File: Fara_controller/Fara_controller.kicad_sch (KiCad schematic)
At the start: 25 parts, among them U1 XL1509-12, U2 LDD-700L, U3 LDD-700L, U4 LDD-700L, U5 LDD-700L, X1 Conn_01x02, X10 Conn_01x02, X11 Conn_01x02, X2 Conn_01x02, X3 Fan_3pin, X4 Fan_3pin, X5 Fan_3pin, X6 Fan_3pin, X7 Joystick, X8 Conn_01x02, X9 Conn_01x02

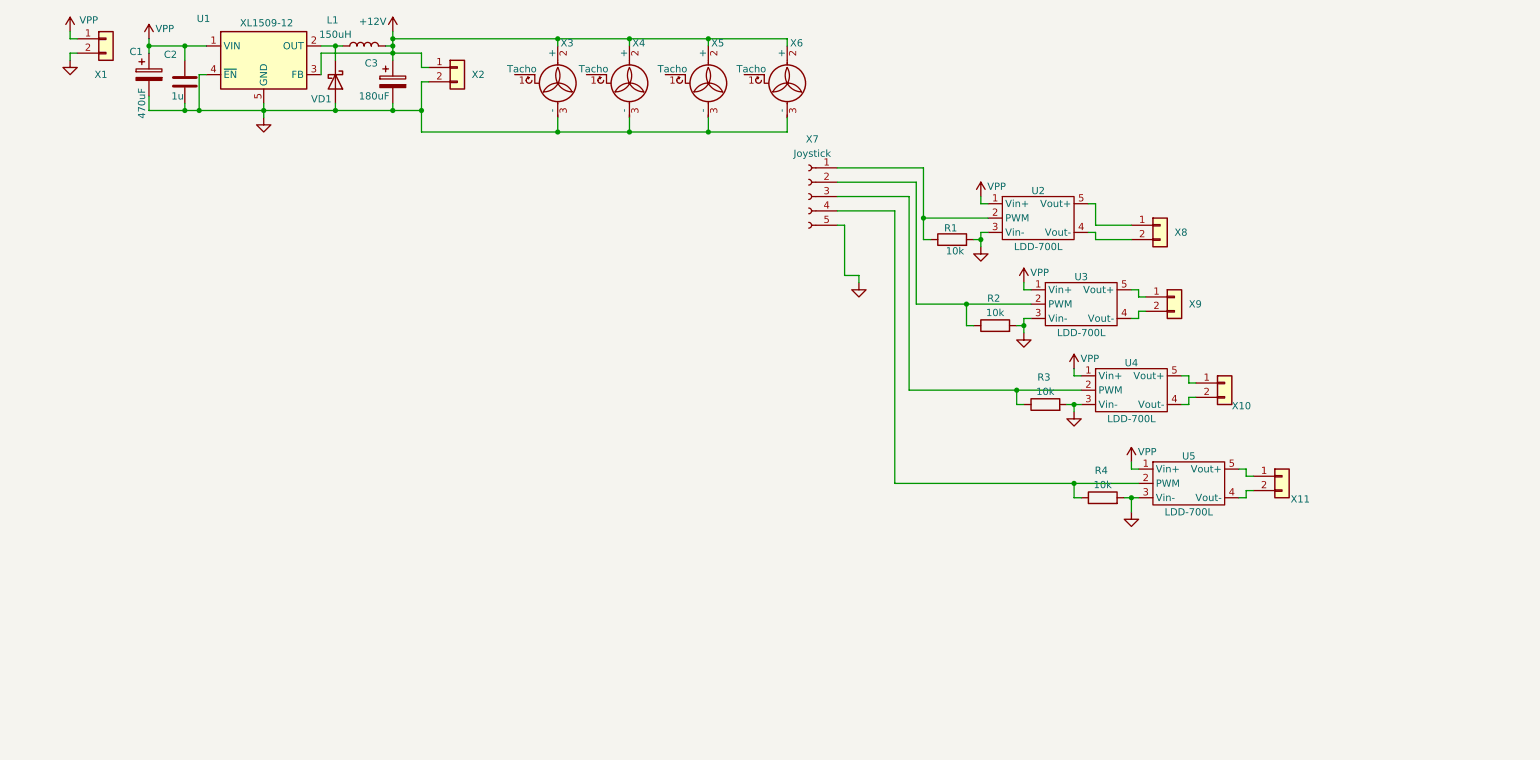
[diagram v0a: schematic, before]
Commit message: v0.2 draft routing of the 24V edition
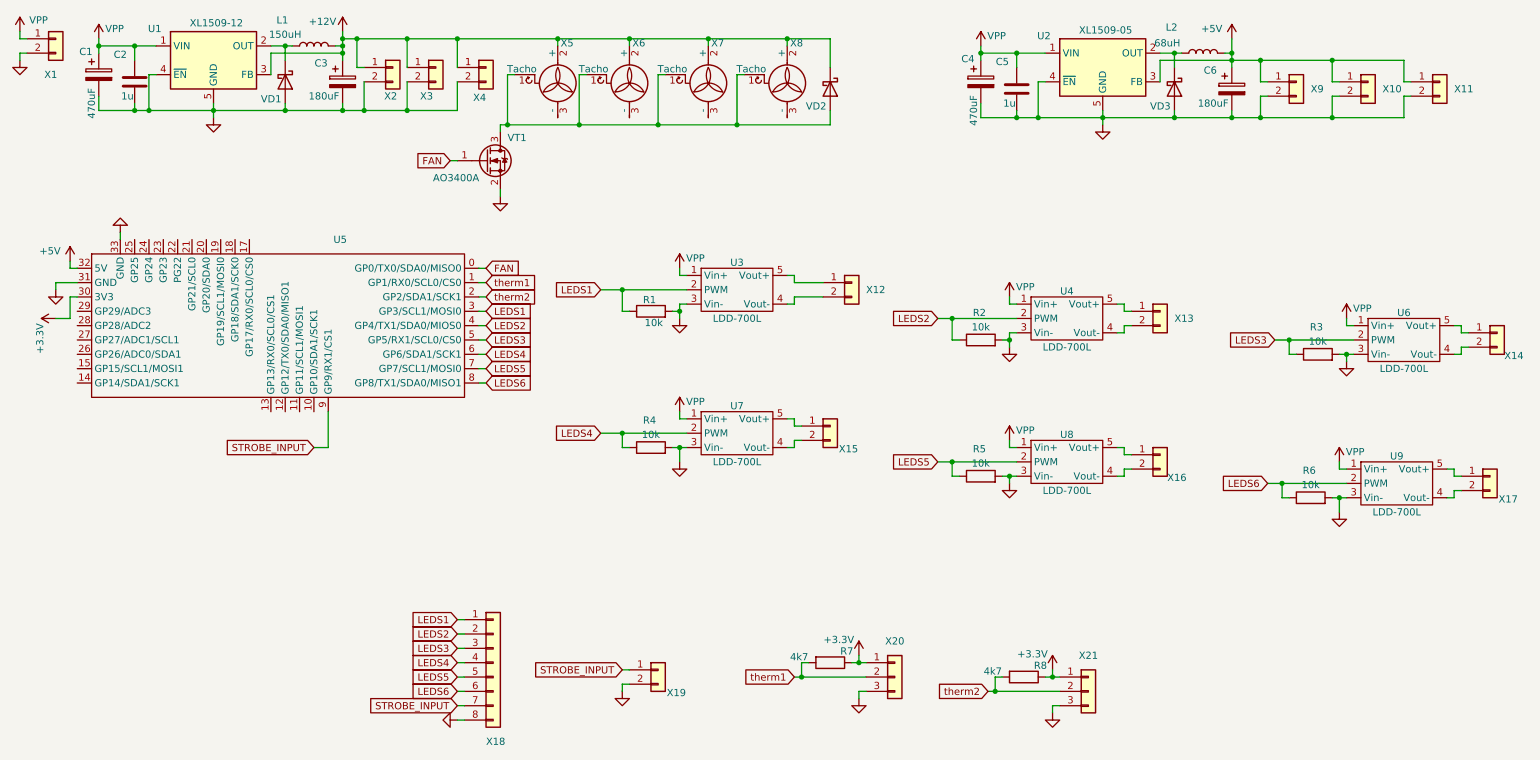
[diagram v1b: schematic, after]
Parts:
- removed X7: Joystick, Connector_JST:JST_XH_B5B-XH-A_1x05_P2.50mm_Vertical, symbol Connector:Conn_01x05_Female
- added C4: 470uF, Capacitor_THT:CP_Radial_D10.0mm_P5.00mm, symbol Device:C_Polarized
- added C5: 1u, Capacitor_SMD:C_0603_1608Metric_Pad1.08x0.95mm_HandSolder, symbol Device:C
- added C6: 180uF, Capacitor_SMD:CP_Elec_6.3x7.7, symbol Device:C_Polarized
- added L2: 68uH, Inductor_SMD:L_Bourns_SRP1050WA, symbol Device:L
- added R5, R6: 10k, Resistor_SMD:R_0603_1608Metric_Pad0.98x0.95mm_HandSolder, symbol Device:R
- added R7, R8: 4k7, Resistor_SMD:R_0603_1608Metric_Pad0.98x0.95mm_HandSolder, symbol Device:R
- added U2: XL1509-05, Package_SO:SOIC-8-1EP_3.9x4.9mm_P1.27mm_EP2.95x4.9mm_Mask2.71x3.4mm_ThermalVias, symbol My_8_lib_sym:XL1509-3.3
- added U5: ~, my8lib:RP2040Zero, symbol Vedro:RP2040-One
- added U8, U9: LDD-700L, my8lib:LDD-700L, symbol Shield_Emergent:LDD-700L
- added VD2, VD3: CDBA3100-HF, Diode_SMD:D_SMA, symbol Diode:CDBA3100-HF
- added VT1: AO3400A, Package_TO_SOT_SMD:SOT-23, symbol Transistor_FET:AO3400A
- added X10, X11, X16, X17, X19, X3, X4, X9: Conn_01x02, Connector_JST:JST_XH_B2B-XH-A_1x02_P2.50mm_Vertical, symbol Connector_Generic:Conn_01x02
- added X18: Objective, Connector_PinSocket_1.27mm:PinSocket_1x08_P1.27mm_Vertical, symbol Connector_Generic:Conn_01x08
- added X20, X21: Conn_01x03, Connector_JST:JST_XH_B3B-XH-A_1x03_P2.50mm_Vertical, symbol Connector_Generic:Conn_01x03
- renumbered U2 to U3, U3 to U4, U4 to U6, U5 to U7, X8 to X12, X9 to X13, X10 to X14, X11 to X15, X3 to X5, X4 to X6, X5 to X7, X6 to X8
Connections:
- net +12V: now also VD2.1 (K), X3.1 (Pin_1), X4.1 (Pin_1)
- net GND: now also C4.2, C5.2, C6.2, R5.2, R6.2, U2.4 (~{EN}), U2.5 (GND), U2.6 (GND), U2.7 (GND), U2.8 (GND), U2.9 (GND), U5.31 (GND), U5.33 (GND), U8.3 (Vin-), U9.3 (Vin-), VD3.2 (A), VT1.2 (S), X10.2 (Pin_2), X11.2 (Pin_2), X18.8 (Pin_8), X19.2 (Pin_2), X20.3 (Pin_3), X21.3 (Pin_3), X3.2 (Pin_2), X4.2 (Pin_2), X9.2 (Pin_2); no longer X5.3 (-), X6.3 (-), X7.3 (-), X8.3 (-)
- net VPP: now also C4.1, C5.1, U2.1 (VIN), U8.1 (Vin+), U9.1 (Vin+)
- net at X6.1 (Tacho): now also X5.1 (Tacho), X7.1 (Tacho), X8.1 (Tacho), VD2.2 (A), VT1.3 (D)
- net LEDS3: now reaches R3.1, U6.2 (PWM)
- net LEDS3: now also U5.5 (GP5/RX1/SCL0/CS0), X18.3 (Pin_3)
- net LEDS2: now reaches R2.1, U4.2 (PWM)
- net LEDS2: now also U5.4 (GP4/TX1/SDA0/MIOS0), X18.2 (Pin_2)
- net LEDS1: now reaches R1.1, U3.2 (PWM)
- net LEDS1: now also U5.3 (GP3/SCL1/MOSI0), X18.1 (Pin_1)
- net LEDS4: now reaches R4.1, U7.2 (PWM)
- net LEDS4: now also U5.6 (GP6/SDA1/SCK1), X18.4 (Pin_4)
- new net: U8.5 (Vout+), X16.1 (Pin_1)
- new net: U8.4 (Vout-), X16.2 (Pin_2)
- new net: U9.4 (Vout-), X17.2 (Pin_2)
- new net: U9.5 (Vout+), X17.1 (Pin_1)
- new net: L2.1, U2.2 (OUT), VD3.1 (K)
- new net +3.3V: R7.1, R8.1, U5.30 (3V3), X20.1 (Pin_1), X21.1 (Pin_1)
- new net +5V: C6.1, L2.2, U2.3 (FB), U5.32 (5V), X10.1 (Pin_1), X11.1 (Pin_1), X9.1 (Pin_1)
- new net FAN: U5.0 (GP0/TX0/SDA0/MISO0), VT1.1 (G)
- new net LEDS5: R5.1, U5.7 (GP7/SCL1/MOSI0), U8.2 (PWM), X18.5 (Pin_5)
- new net LEDS6: R6.1, U5.8 (GP8/TX1/SDA0/MISO1), U9.2 (PWM), X18.6 (Pin_6)
- new net STROBE_INPUT: U5.9 (GP9/RX1/CS1), X18.7 (Pin_7), X19.1 (Pin_1)
- new net therm1: R7.2, U5.1 (GP1/RX0/SCL0/CS0), X20.2 (Pin_2)
- new net therm2: R8.2, U5.2 (GP2/SDA1/SCK1), X21.2 (Pin_2)
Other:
- moved on the sheet: C1, C2, C3, L1, R1, R2, R3, R4, U1, U3, U4, U6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

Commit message: v0.3 Seems 2B ready
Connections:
- net FAN: now also U5.12 (GP12/TX0/SDA0/MISO1); no longer U5.0 (GP0/TX0/SDA0/MISO0)
- net LEDS1: now also U5.29 (GP29/ADC3); no longer U5.3 (GP3/SCL1/MOSI0)
- net LEDS2: now also U5.28 (GP28/ADC2); no longer U5.4 (GP4/TX1/SDA0/MIOS0)
- net LEDS3: now also U5.27 (GP27/ADC1/SCL1); no longer U5.5 (GP5/RX1/SCL0/CS0)
- net LEDS4: now also U5.26 (GP26/ADC0/SDA1); no longer U5.6 (GP6/SDA1/SCK1)
- net LEDS5: now also U5.15 (GP15/SCL1/MOSI1); no longer U5.7 (GP7/SCL1/MOSI0)
- net LEDS6: now also U5.14 (GP14/SDA1/SCK1); no longer U5.8 (GP8/TX1/SDA0/MISO1)
- net STROBE_INPUT: now also U5.13 (GP13/RX0/SCL0/CS1); no longer U5.9 (GP9/RX1/CS1)
